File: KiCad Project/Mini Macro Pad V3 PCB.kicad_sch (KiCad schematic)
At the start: 55 parts, among them J1 USB_C_Receptacle_USB2.0_14P, SW1 SW_Push bootsel, SW10 SW_Push, SW11 SW_Push, SW12 SW_Push, SW13 SW_Push, SW14 SW_Push, SW15 SW_Push, SW16 SW_Push, SW17 SW_Push, SW18 SW_Push, SW19 SW_Push, SW2 SW_Push, SW20 SW_Push, SW21 SW_Push, SW22 RotaryEncoder_Switch_MP, SW23 RotaryEncoder_Switch_MP, SW3 SW_Push, SW4 SW_Push, SW5 SW_Push, SW6 SW_Push, SW7 SW_Push, SW8 SW_Push, SW9 SW_Push, U1 RP2040, U2 NCP1117-3.3_SOT223, U3 W25Q128JVS, Y1 ABM8-272-T3

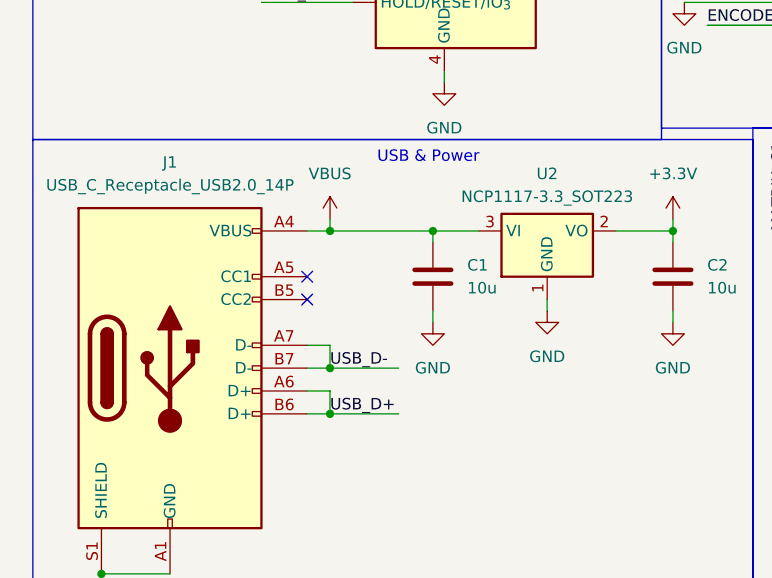
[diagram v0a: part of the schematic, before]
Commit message: added to usb power
added 5.1k resistors to CC1 & CC2
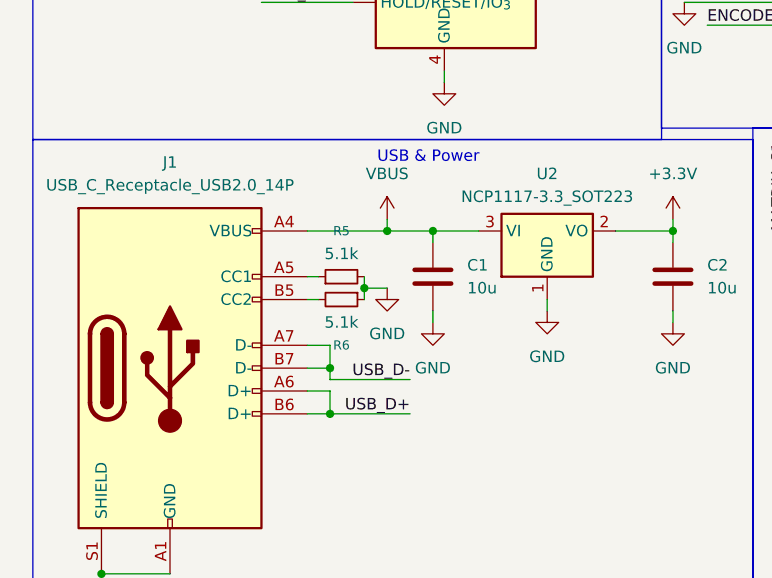
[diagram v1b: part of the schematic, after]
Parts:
- added R5, R6: 5.1k, symbol Device:R_Small
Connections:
- net GND: now also R5.2, R6.1
- net at J1.A5 (CC1): now also R5.1
- net at J1.B5 (CC2): now also R6.2
- no-connect marks 2 -> 0

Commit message: Assigned footprints to all components
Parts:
- added TP1: SWCLK, TestPoint:TestPoint_Pad_2.5x2.5mm, symbol Connector:TestPoint
- added TP2: SWD, TestPoint:TestPoint_Pad_2.5x2.5mm, symbol Connector:TestPoint
- C1, C11, C12, C13, C2, C3, C4, C5, C6, C7, C8: footprint (none) -> Capacitor_SMD:C_0402_1005Metric_Pad0.74x0.62mm_HandSolder
- J1: footprint (none) -> Connector_USB:USB_C_Receptacle_GCT_USB4125-xx-x-0190_6P_TopMnt_Horizontal
- R1, R2, R3, R4, R5, R6: footprint (none) -> Capacitor_SMD:C_0603_1608Metric_Pad1.08x0.95mm_HandSolder
- SW1: footprint (none) -> Button_Switch_SMD:Panasonic_EVQPUK_EVQPUB
- SW10, SW11, SW12, SW13, SW14, SW15, SW16, SW17, SW18, SW19, SW2, SW20, SW21, SW3, SW4, SW5, SW6, SW7, SW8, SW9: footprint (none) -> Button_Switch_THT:SW_PUSH_6mm_H4.3mm
- SW22, SW23: footprint (none) -> Rotary_Encoder:RotaryEncoder_Bourns_Horizontal_PEL12D-2x16F-Sxxxx
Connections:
- net GND: now also U1.19 (TESTEN)
- net XOUT: now also Y1.3
- net at U1.24 (SWCLK): now also TP1.1
- net at U1.25 (SWD): now also TP2.1
- no-connect marks 0 -> 16

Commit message: created PCB & did rough layout
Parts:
- J1: footprint Connector_USB:USB_C_Receptacle_GCT_USB4125-xx-x-0190_6P_TopMnt_Horizontal -> Connector_USB:USB_C_Receptacle_HCTL_HC-TYPE-C-16P-01A
- R1, R2, R3, R4, R5, R6: footprint Capacitor_SMD:C_0603_1608Metric_Pad1.08x0.95mm_HandSolder -> Resistor_SMD:R_0402_1005Metric_Pad0.72x0.64mm_HandSolder
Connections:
- net XOUT: no longer C13.2, R2.1, Y1.3
- new net: C13.2, R2.1, Y1.3
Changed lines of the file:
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@@
 	)
 	(junction
-		(at 44.45 80.01)
-		(diameter 0)
-		(color 0 0 0 0)
-	)
-	(junction
 		(at 96.52 185.42)
 		(diameter 0)
@@
 	)
 	(junction
-		(at 39.37 80.01)
-		(diameter 0)
-		(color 0 0 0 0)
-	)
-	(junction
 		(at 144.78 156.21)
 		(diameter 0)
@@
 	(wire
 		(pts
-			(xy 39.37 80.01) (xy 44.45 80.01)
-		)
-		(stroke
-			(width 0)
-			(type default)
-		)
-	)
-	(wire
-		(pts
 			(xy 44.45 80.01) (xy 50.8 80.01)
 		)
@@
 			)
 		)
-		(property "Footprint" "Capacitor_SMD:C_0603_1608Metric_Pad1.08x0.95mm_HandSolder"
+		(property "Footprint" "Resistor_SMD:R_0402_1005Metric_Pad0.72x0.64mm_HandSolder"
 			(at 171.45 73.66 0)
 			(effects
@@
 			)
 		)
-		(property "Footprint" "Capacitor_SMD:C_0603_1608Metric_Pad1.08x0.95mm_HandSolder"
+		(property "Footprint" "Resistor_SMD:R_0402_1005Metric_Pad0.72x0.64mm_HandSolder"
 			(at 41.91 80.01 0)
 			(effects
@@
 			)
 		)
-		(property "Footprint" "Capacitor_SMD:C_0603_1608Metric_Pad1.08x0.95mm_HandSolder"
+		(property "Footprint" "Resistor_SMD:R_0402_1005Metric_Pad0.72x0.64mm_HandSolder"
 			(at 46.99 158.75 0)
 			(effects
@@
 			)
 		)
-		(property "Footprint" "Capacitor_SMD:C_0603_1608Metric_Pad1.08x0.95mm_HandSolder"
+		(property "Footprint" "Resistor_SMD:R_0402_1005Metric_Pad0.72x0.64mm_HandSolder"
 			(at 171.45 81.28 0)
 			(effects
@@
 			)
 		)
-		(property "Footprint" "Capacitor_SMD:C_0603_1608Metric_Pad1.08x0.95mm_HandSolder"
+		(property "Footprint" "Resistor_SMD:R_0402_1005Metric_Pad0.72x0.64mm_HandSolder"
 			(at 31.75 113.03 0)
 			(effects
@@
 			)
 		)
-		(property "Footprint" "Capacitor_SMD:C_0603_1608Metric_Pad1.08x0.95mm_HandSolder"
+		(property "Footprint" "Resistor_SMD:R_0402_1005Metric_Pad0.72x0.64mm_HandSolder"
 			(at 46.99 156.21 0)
 			(effects
@@
 			)
 		)
-		(property "Footprint" "Connector_USB:USB_C_Receptacle_GCT_USB4125-xx-x-0190_6P_TopMnt_Horizontal"
+		(property "Footprint" "Connector_USB:USB_C_Receptacle_HCTL_HC-TYPE-C-16P-01A"
 			(at 31.75 166.37 0)
 			(effects

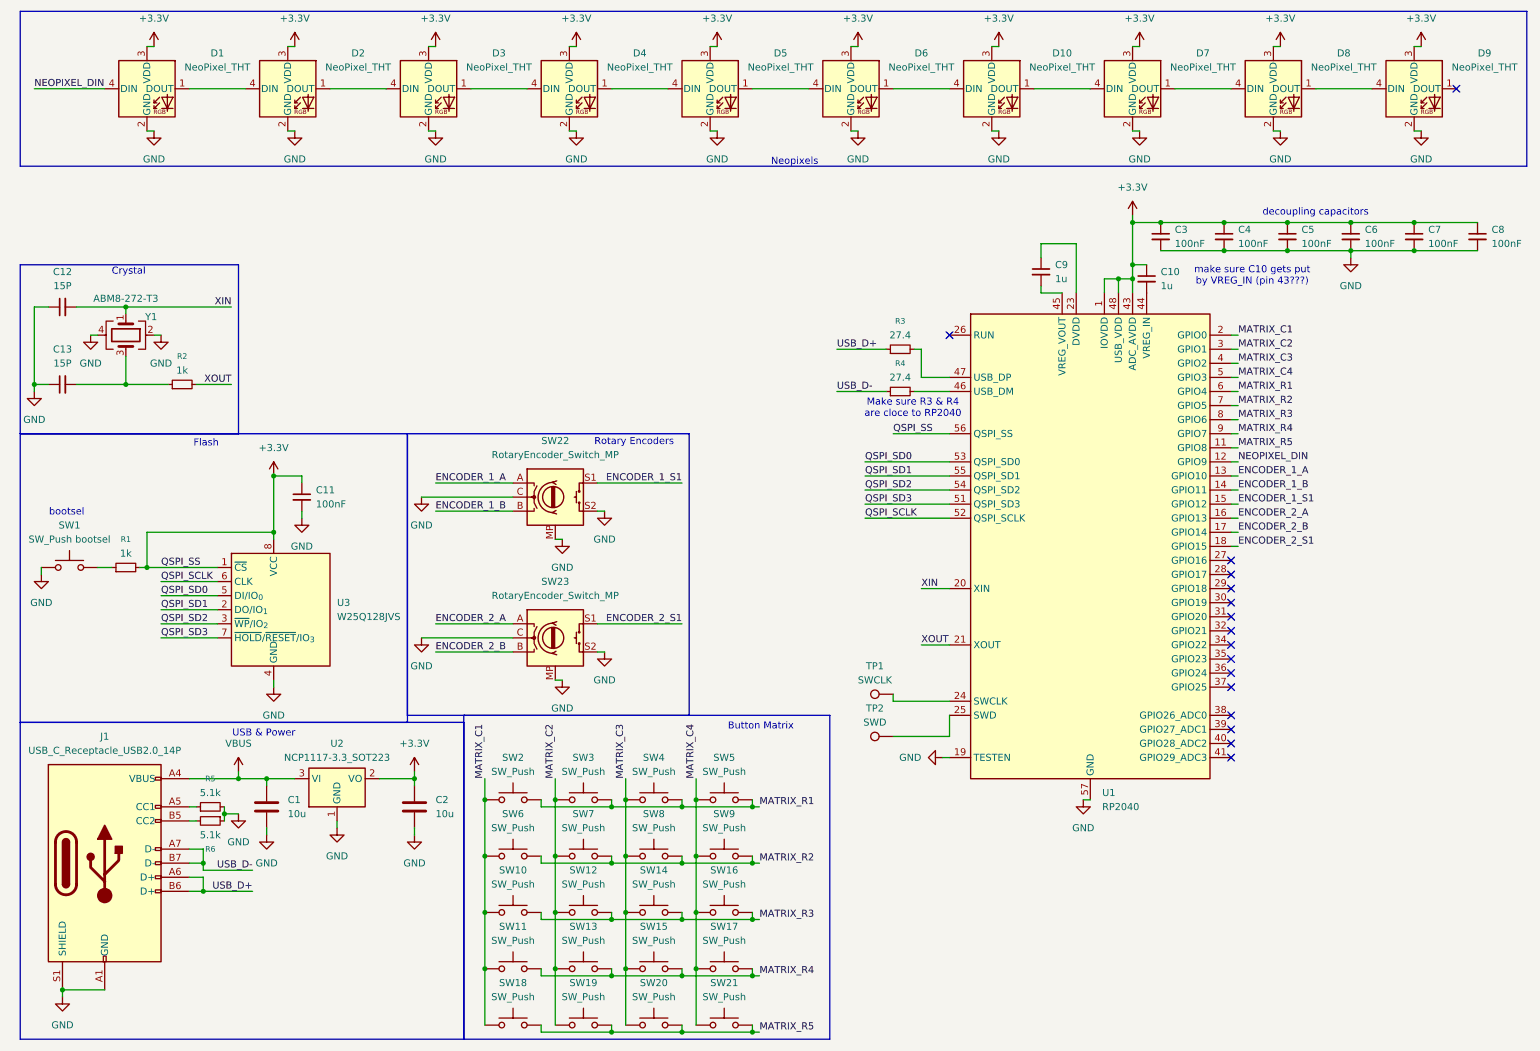
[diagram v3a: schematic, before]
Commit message: added test points & fixed layout issues with buttons
some buttons were numbered in the wrong order.
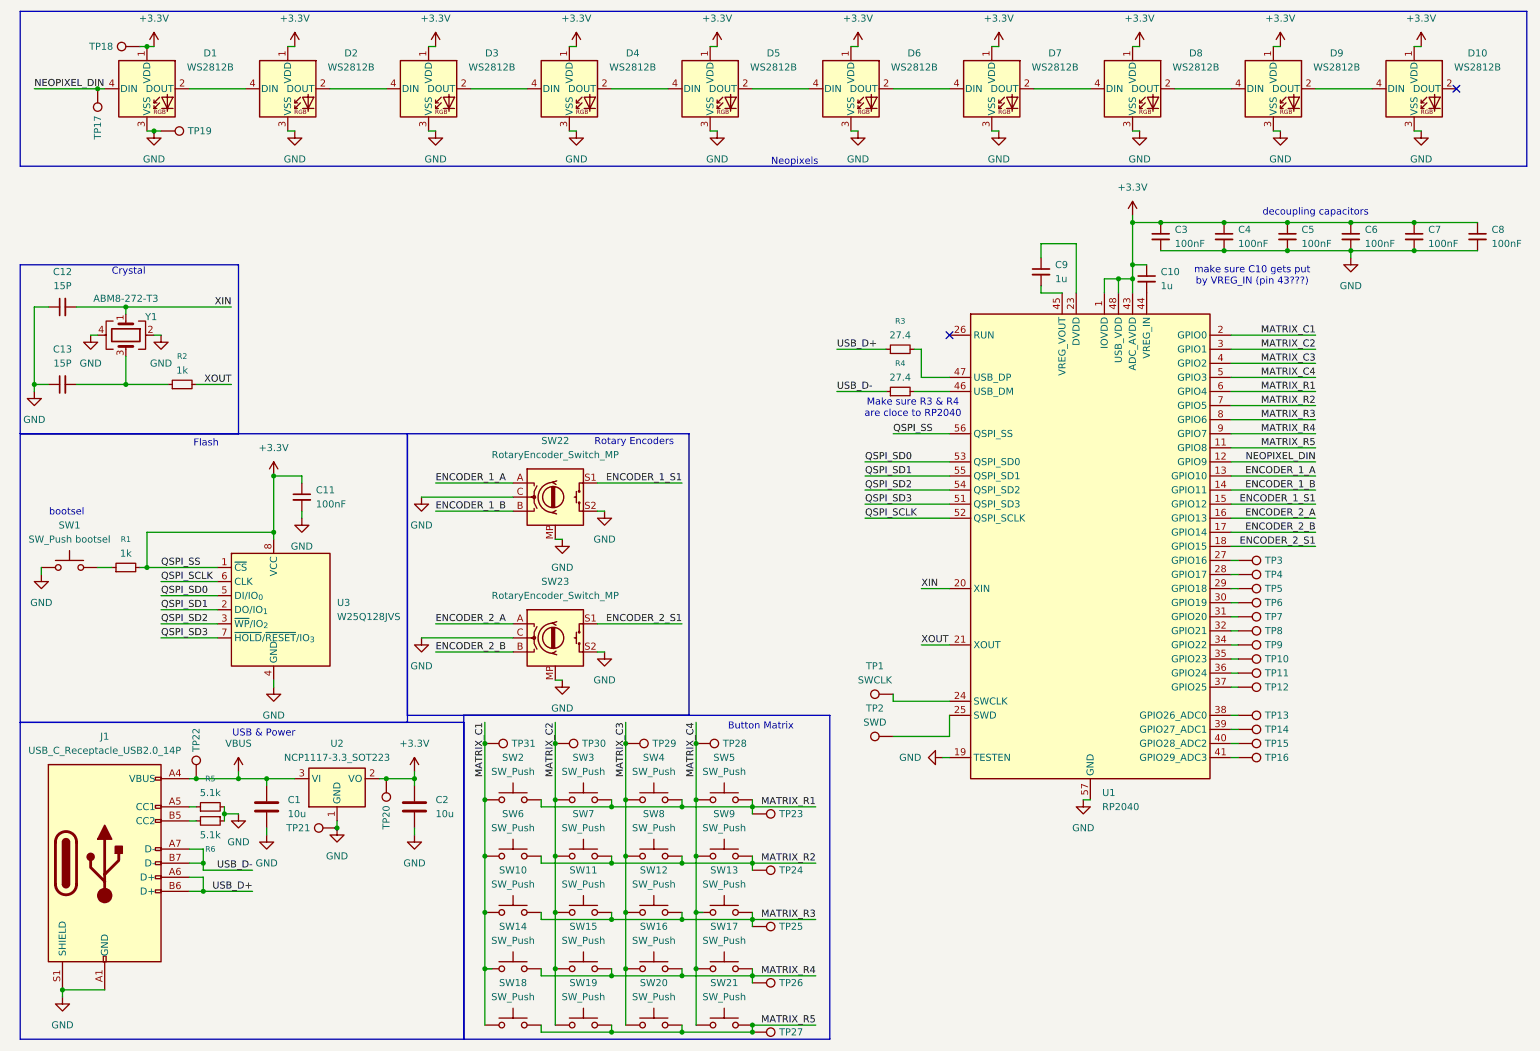
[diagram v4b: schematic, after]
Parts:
- removed D1, D10, D2, D3, D4, D5, D6, D7, D8, D9: NeoPixel_THT, LED_SMD:LED_SK6812_PLCC4_5.0x5.0mm_P3.2mm, symbol LED:NeoPixel_THT
- added D1, D10, D2, D3, D4, D5, D6, D7, D8, D9: WS2812B, LED_SMD:LED_WS2812B_PLCC4_5.0x5.0mm_P3.2mm, symbol LED:WS2812B
- added TP10, TP11, TP12, TP13, TP14, TP15, TP16, TP17, TP18, TP19, TP20, TP21, TP22, TP23, TP24, TP25, TP26, TP27, TP28, TP29, TP3, TP30, TP31, TP4, TP5, TP6, TP7, TP8, TP9: ~, TestPoint:TestPoint_Pad_1.5x1.5mm, symbol Connector:TestPoint
- TP1, TP2: footprint TestPoint:TestPoint_Pad_2.5x2.5mm -> TestPoint:TestPoint_Pad_1.5x1.5mm
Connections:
- net +3.3V: now also D1.1 (VDD), D10.1 (VDD), D2.1 (VDD), D3.1 (VDD), D4.1 (VDD), D5.1 (VDD), D6.1 (VDD), D7.1 (VDD), D8.1 (VDD), D9.1 (VDD), TP18.1, TP20.1
- net GND: now also D1.3 (VSS), D10.3 (VSS), D2.3 (VSS), D3.3 (VSS), D4.3 (VSS), D5.3 (VSS), D6.3 (VSS), D7.3 (VSS), D8.3 (VSS), D9.3 (VSS), TP19.1, TP21.1
- net MATRIX_C1: now also SW14.1, TP31.1; no longer SW11.1
- net MATRIX_C2: now also SW11.1, SW15.1, TP30.1; no longer SW12.1, SW13.1
- net MATRIX_C3: now also SW12.1, SW16.1, TP29.1; no longer SW14.1, SW15.1
- net MATRIX_C4: now also SW13.1, TP28.1; no longer SW16.1
- net MATRIX_R1: now also TP23.1
- net MATRIX_R2: now also TP24.1
- net MATRIX_R3: now also SW11.2, SW13.2, TP25.1; no longer SW14.2, SW16.2
- net MATRIX_R4: now also SW14.2, SW16.2, TP26.1; no longer SW11.2, SW13.2
- net MATRIX_R5: now also TP27.1
- net NEOPIXEL_DIN: now also D1.4 (DIN), TP17.1
- net VBUS: now also TP22.1
- net at U1.27 (GPIO16): now also TP3.1
- net at U1.28 (GPIO17): now also TP4.1
- net at U1.29 (GPIO18): now also TP5.1
- net at U1.30 (GPIO19): now also TP6.1
- net at U1.31 (GPIO20): now also TP7.1
- net at U1.32 (GPIO21): now also TP8.1
- net at U1.34 (GPIO22): now also TP9.1
- net at U1.35 (GPIO23): now also TP10.1
- net at U1.36 (GPIO24): now also TP11.1
- net at U1.37 (GPIO25): now also TP12.1
- net at U1.38 (GPIO26_ADC0): now also TP13.1
- net at U1.39 (GPIO27_ADC1): now also TP14.1
- net at U1.40 (GPIO28_ADC2): now also TP15.1
- net at U1.41 (GPIO29_ADC3): now also TP16.1
- new net: D10.4 (DIN), D9.2 (DOUT)
- new net: D6.2 (DOUT), D7.4 (DIN)
- new net: D5.2 (DOUT), D6.4 (DIN)
- new net: D4.2 (DOUT), D5.4 (DIN)
- new net: D2.2 (DOUT), D3.4 (DIN)
- new net: D1.2 (DOUT), D2.4 (DIN)
- new net: D3.2 (DOUT), D4.4 (DIN)
- new net: D8.2 (DOUT), D9.4 (DIN)
- new net: D7.2 (DOUT), D8.4 (DIN)
- no-connect marks 16 -> 2
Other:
- moved on the sheet: SW11, SW12, SW13, SW14, SW15, SW16

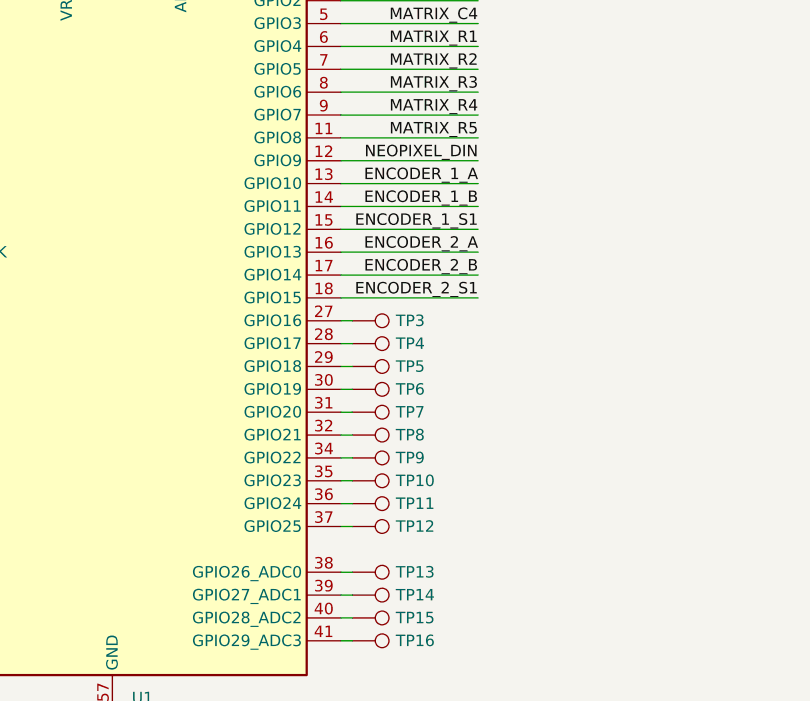
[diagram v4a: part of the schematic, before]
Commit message: changed GPIO pins used
moved rotary encoder GPIO pins away from the pins used for the crystal to prevent stability issues
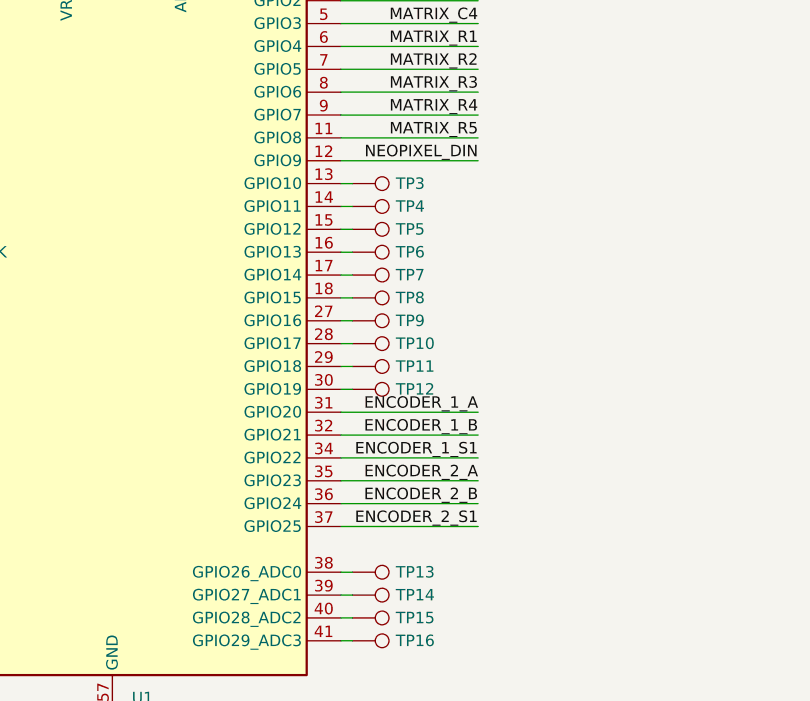
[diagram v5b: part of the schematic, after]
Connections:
- net ENCODER_1_A: now also U1.31 (GPIO20); no longer U1.13 (GPIO10)
- net ENCODER_1_B: now also U1.32 (GPIO21); no longer U1.14 (GPIO11)
- net ENCODER_1_S1: now also U1.34 (GPIO22); no longer U1.15 (GPIO12)
- net ENCODER_2_A: now also U1.35 (GPIO23); no longer U1.16 (GPIO13)
- net ENCODER_2_B: now also U1.36 (GPIO24); no longer U1.17 (GPIO14)
- net ENCODER_2_S1: now also U1.37 (GPIO25); no longer U1.18 (GPIO15)
- net at TP11.1: now also U1.29 (GPIO18); no longer U1.36 (GPIO24)
- net at TP7.1: now also U1.17 (GPIO14); no longer U1.31 (GPIO20)
- net at TP12.1: now also U1.30 (GPIO19); no longer U1.37 (GPIO25)
- net at TP5.1: now also U1.15 (GPIO12); no longer U1.29 (GPIO18)
- net at TP6.1: now also U1.16 (GPIO13); no longer U1.30 (GPIO19)
- net at TP4.1: now also U1.14 (GPIO11); no longer U1.28 (GPIO17)
- net at TP9.1: now also U1.27 (GPIO16); no longer U1.34 (GPIO22)
- net at TP8.1: now also U1.18 (GPIO15); no longer U1.32 (GPIO21)
- net at TP3.1: now also U1.13 (GPIO10); no longer U1.27 (GPIO16)
- net at TP10.1: now also U1.28 (GPIO17); no longer U1.35 (GPIO23)
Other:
- moved on the sheet: TP10, TP11, TP12, TP3, TP4, TP5, TP6, TP7, TP8, TP9

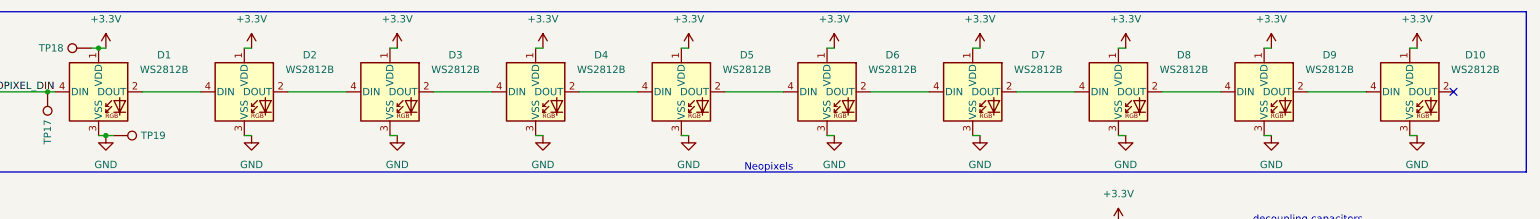
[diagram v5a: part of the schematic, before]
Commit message: added decoupling capacitors for neopixels
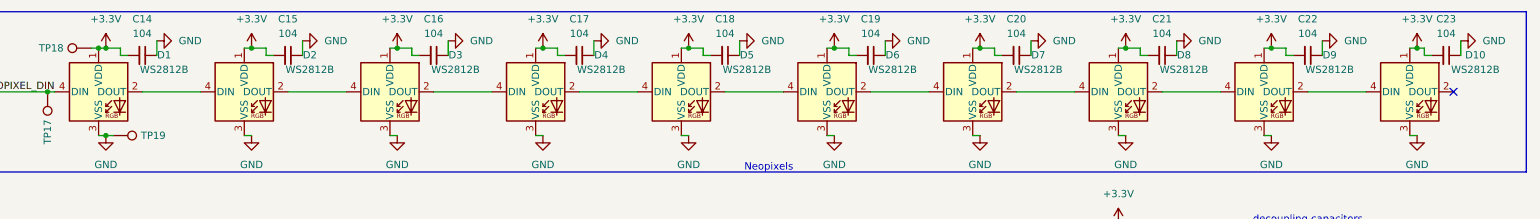
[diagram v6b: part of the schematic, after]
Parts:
- added C14, C15, C16, C17, C18, C19, C20, C21, C22, C23: 104, Capacitor_SMD:C_0402_1005Metric_Pad0.74x0.62mm_HandSolder, symbol Device:C_Small
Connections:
- net +3.3V: now also C14.2, C15.2, C16.2, C17.2, C18.2, C19.2, C20.2, C21.2, C22.2, C23.2
- net GND: now also C14.1, C15.1, C16.1, C17.1, C18.1, C19.1, C20.1, C21.1, C22.1, C23.1

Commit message: Started drawing traces
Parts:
- SW22, SW23: footprint Rotary_Encoder:RotaryEncoder_Bourns_Horizontal_PEL12D-2x16F-Sxxxx -> Rotary_Encoder:RotaryEncoder_Bourns_Horizontal_PEC12R-2x17F-Sxxxx
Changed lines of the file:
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@@
 			)
 		)
-		(property "Footprint" "Rotary_Encoder:RotaryEncoder_Bourns_Horizontal_PEL12D-2x16F-Sxxxx"
+		(property "Footprint" "Rotary_Encoder:RotaryEncoder_Bourns_Horizontal_PEC12R-2x17F-Sxxxx"
 			(at 105.41 121.666 0)
 			(effects
@@
 			)
 		)
-		(property "Footprint" "Rotary_Encoder:RotaryEncoder_Bourns_Horizontal_PEL12D-2x16F-Sxxxx"
+		(property "Footprint" "Rotary_Encoder:RotaryEncoder_Bourns_Horizontal_PEC12R-2x17F-Sxxxx"
 			(at 105.41 96.266 0)
 			(effects
